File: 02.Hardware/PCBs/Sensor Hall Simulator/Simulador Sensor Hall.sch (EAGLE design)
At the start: 29 parts

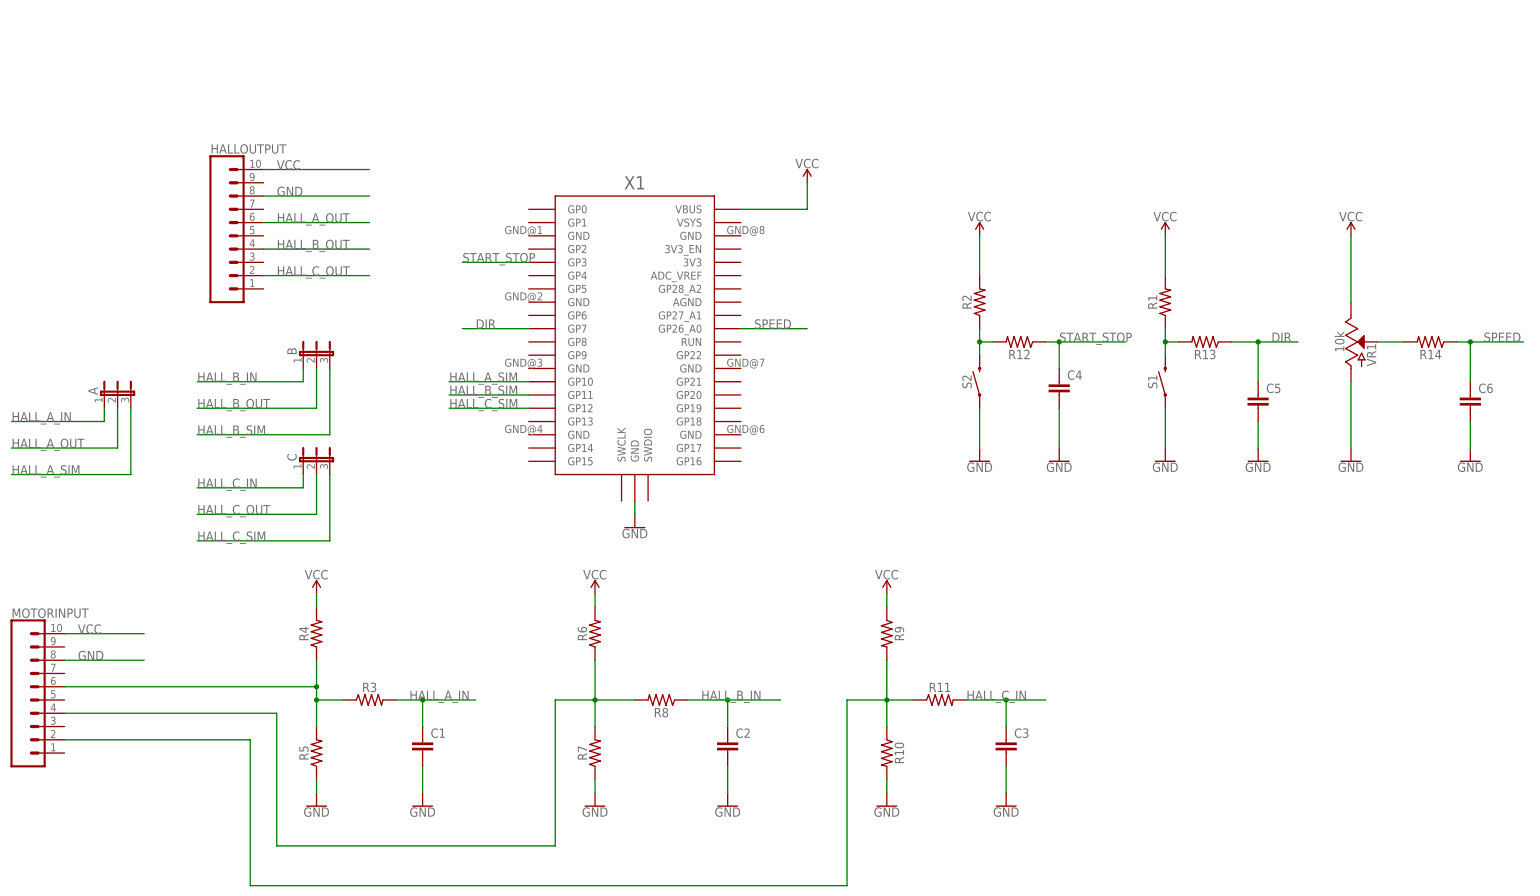
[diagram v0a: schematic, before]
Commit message: v2 Simulador Sensor Hall
Eliminacion de conector de entrada sensores Hall.
Reduccion de tamaño.
Cambio del conector de entrada/salida
Correccion de errores
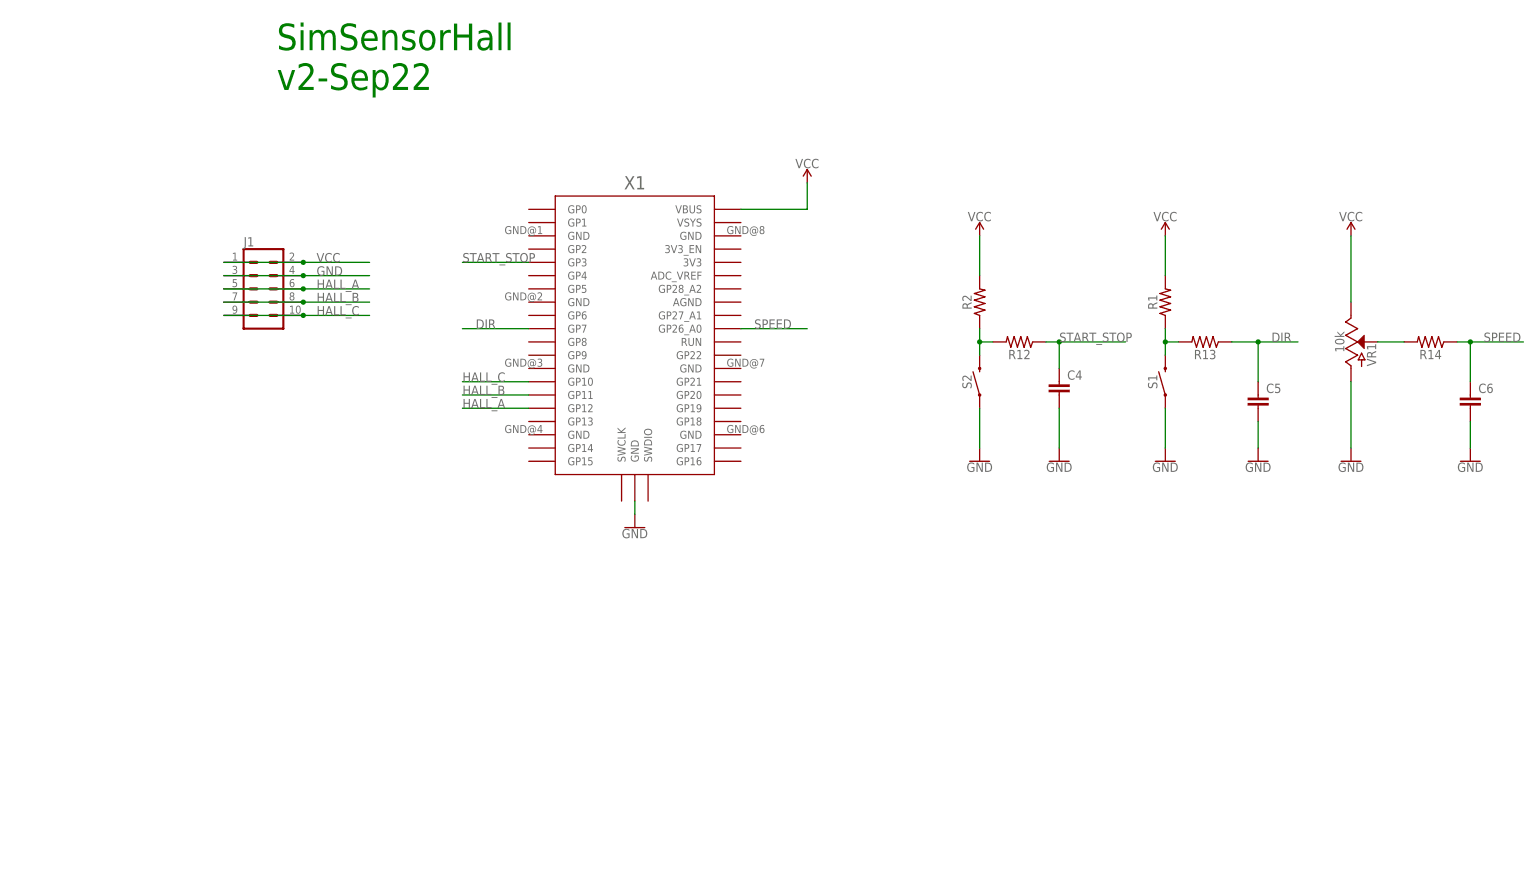
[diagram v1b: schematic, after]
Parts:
- removed A, B, C: (no value), jumper:JP2E
- removed C1, C2, C3: (no value), rcl:C-EUC0805K
- removed HALLOUTPUT, MOTORINPUT: (no value), SparkFun-Connectors:CONN_10"
- removed R10, R11, R3, R4, R5, R6, R7, R8, R9: (no value), SparkFun-Resistors:RESISTOR0805
- added J1: (no value), SparkFun-Connectors:CONN_05X2PTH
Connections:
- removed net HALL_A_IN: A.1, C1.1, R3.2
- removed net HALL_A_OUT: A.2, HALLOUTPUT.6
- removed net HALL_A_SIM: A.3, X1.GP10
- removed net HALL_B_IN: B.1, C2.1, R8.1
- removed net HALL_B_OUT: B.2, HALLOUTPUT.4
- removed net HALL_B_SIM: B.3, X1.GP11
- removed net HALL_C_IN: C.1, C3.1, R11.2
- removed net HALL_C_OUT: C.2, HALLOUTPUT.2
- removed net HALL_C_SIM: C.3, X1.GP12
- removed net N$1: MOTORINPUT.6, R3.1, R4.1, R5.2
- removed net N$2: MOTORINPUT.4, R6.1, R7.2, R8.2
- removed net N$3: MOTORINPUT.2, R10.1, R11.1, R9.2
- new net HALL_A: J1.5, J1.6, X1.GP12
- new net HALL_B: J1.7, J1.8, X1.GP11
- new net HALL_C: J1.10, J1.9, X1.GP10
- net GND: now also J1.3, J1.4; no longer C1.2, C2.2, C3.2, HALLOUTPUT.8, MOTORINPUT.8, R10.2, R5.1, R7.1
- net VCC: now also J1.1, J1.2; no longer HALLOUTPUT.10, MOTORINPUT.10, R4.2, R6.2, R9.1
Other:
- note added: "SimSensorHall v2-Sep22"
